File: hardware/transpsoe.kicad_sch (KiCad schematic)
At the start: 54 parts, among them J12 Conn_01x08_Female, J13 Conn_01x08_Female, J14 Conn_01x08_Male, J15 Conn_01x08_Male, J7 Conn_02x05_Odd_Even, U1 OPA4991, U2 OPA4991, U3 OPA4991

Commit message: Fix 3d models and migrate to KiCad6 R/C footprints
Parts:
- C1, C13, C14, C2, C3, C4, C5, C6: footprint Capacitor_SMD:C_0603_1608Metric_Pad1.05x0.95mm_HandSolder -> Capacitor_SMD:C_0603_1608Metric_Pad1.08x0.95mm_HandSolder
- R1, R10, R11, R12, R13, R14, R2, R20, R21, R22, R23, R25, R26, R27, R28, R29, R30, R31, R32, R33, R34, R35, R4, R40, R41, R42, R43, R44, R45, R46, R47, R49, R5, R6, R7, R9: footprint Resistor_SMD:R_0603_1608Metric_Pad1.05x0.95mm_HandSolder -> Resistor_SMD:R_0603_1608Metric_Pad0.98x0.95mm_HandSolder

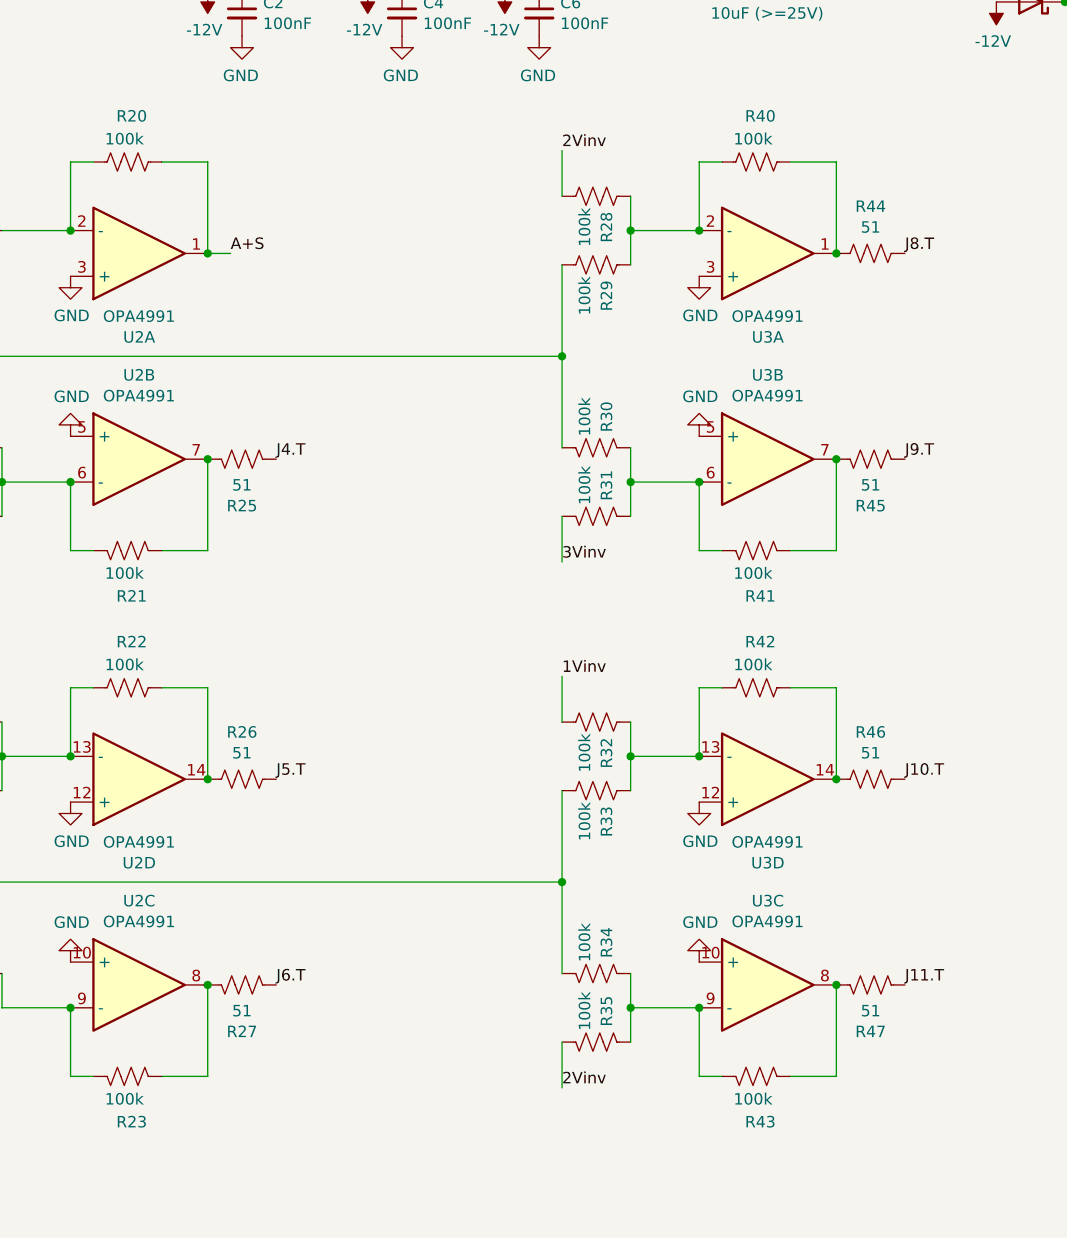
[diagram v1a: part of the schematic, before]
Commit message: Redesign output circuits
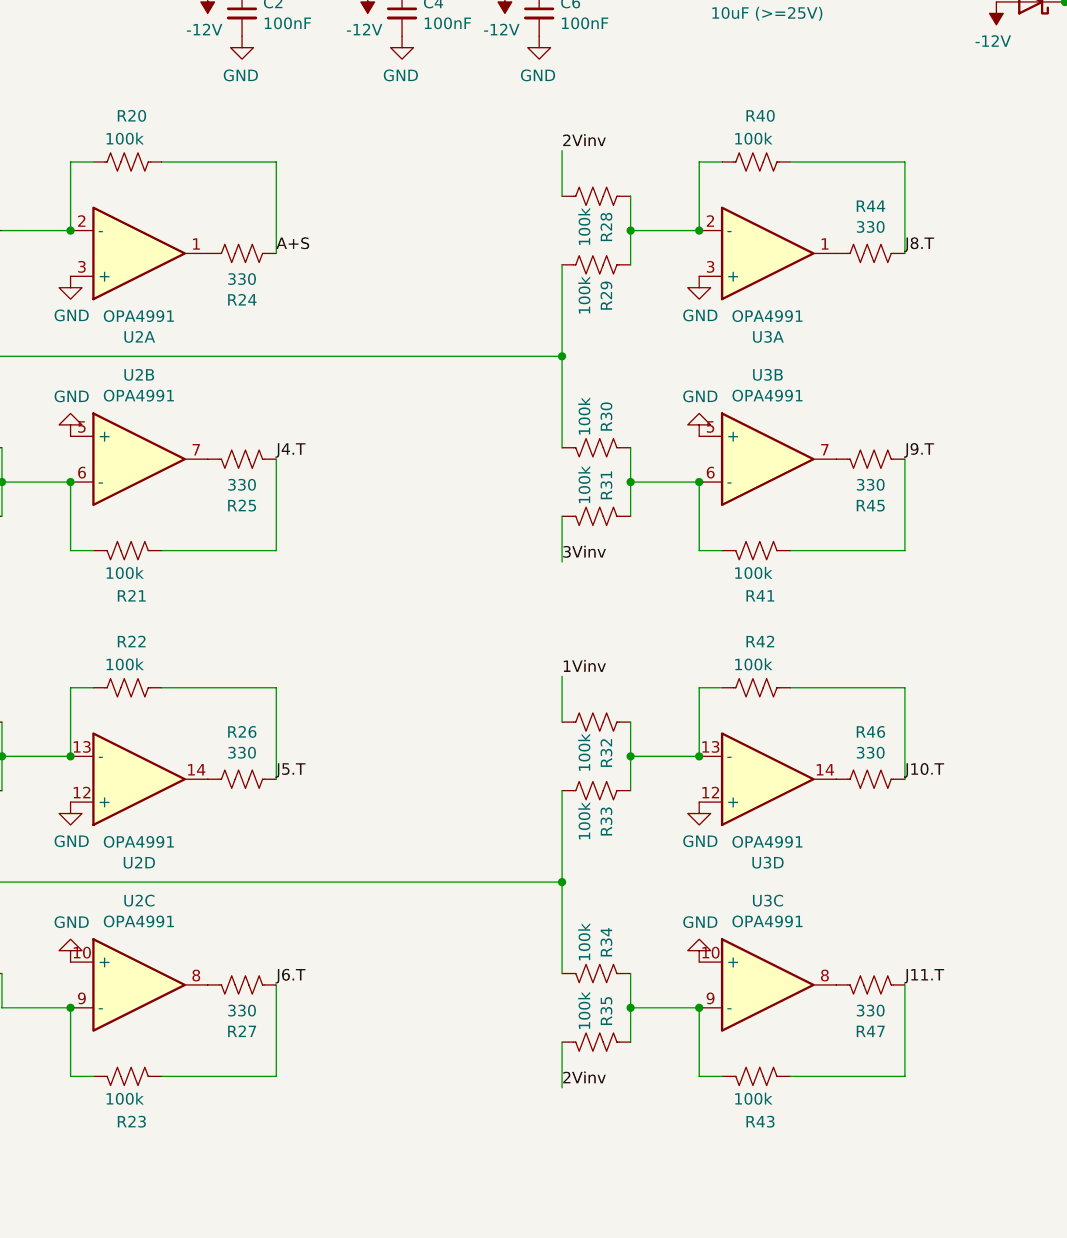
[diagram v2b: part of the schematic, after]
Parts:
- added R24: 330, Resistor_SMD:R_0603_1608Metric_Pad0.98x0.95mm_HandSolder, symbol Device:R_US
- R25, R26, R27, R44, R45, R46, R47: value 51 -> 330
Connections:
- net A+S: now also R24.1; no longer U2.1
- net J10.T: now also R42.1
- net J11.T: now also R43.1
- net J4.T: now also R21.1
- net J5.T: now also R22.1
- net J6.T: now also R23.1
- net J8.T: now also R40.1
- net J9.T: now also R41.1
- net at R25.1, U2.7: no longer R21.1
- net at R44.1, U3.1: no longer R40.1
- net at R45.1, U3.7: no longer R41.1
- net at R26.1, U2.14: no longer R22.1
- net at R27.1, U2.8: no longer R23.1
- net at R46.1, U3.14: no longer R42.1
- net at R47.1, U3.8: no longer R43.1
- new net: R24.2, U2.1
